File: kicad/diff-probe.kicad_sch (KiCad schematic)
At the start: 31 parts, among them IC3 LMH6702, IC4 LMH6702, IC5 LMH6702, J1 Molex 502439-0400, J3 HEADER-1X2CARD-EDGE, J4 Molex 502494-0470, X2 SMA--BU-SMA-H

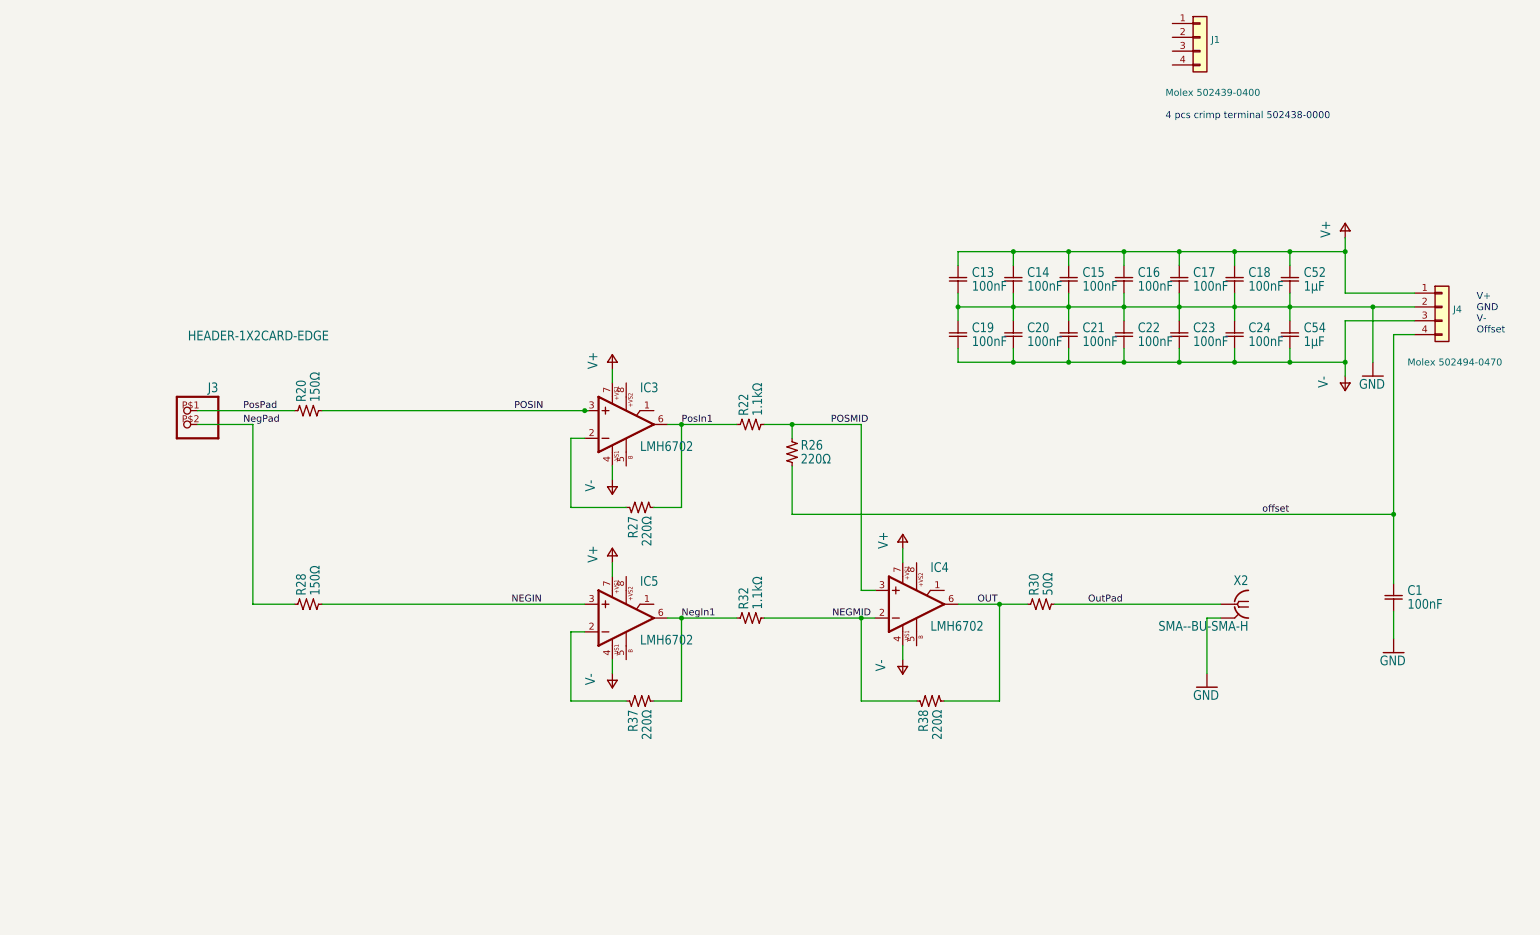
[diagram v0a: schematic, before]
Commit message: Change name for the old project to the kicad_old, remove old stored files. Create new design use new faster op-amp, and two op-amp differential input, create simulation for it. Update PCB design. Still need to design the PCB file, and check the simulation result - need some optimization.
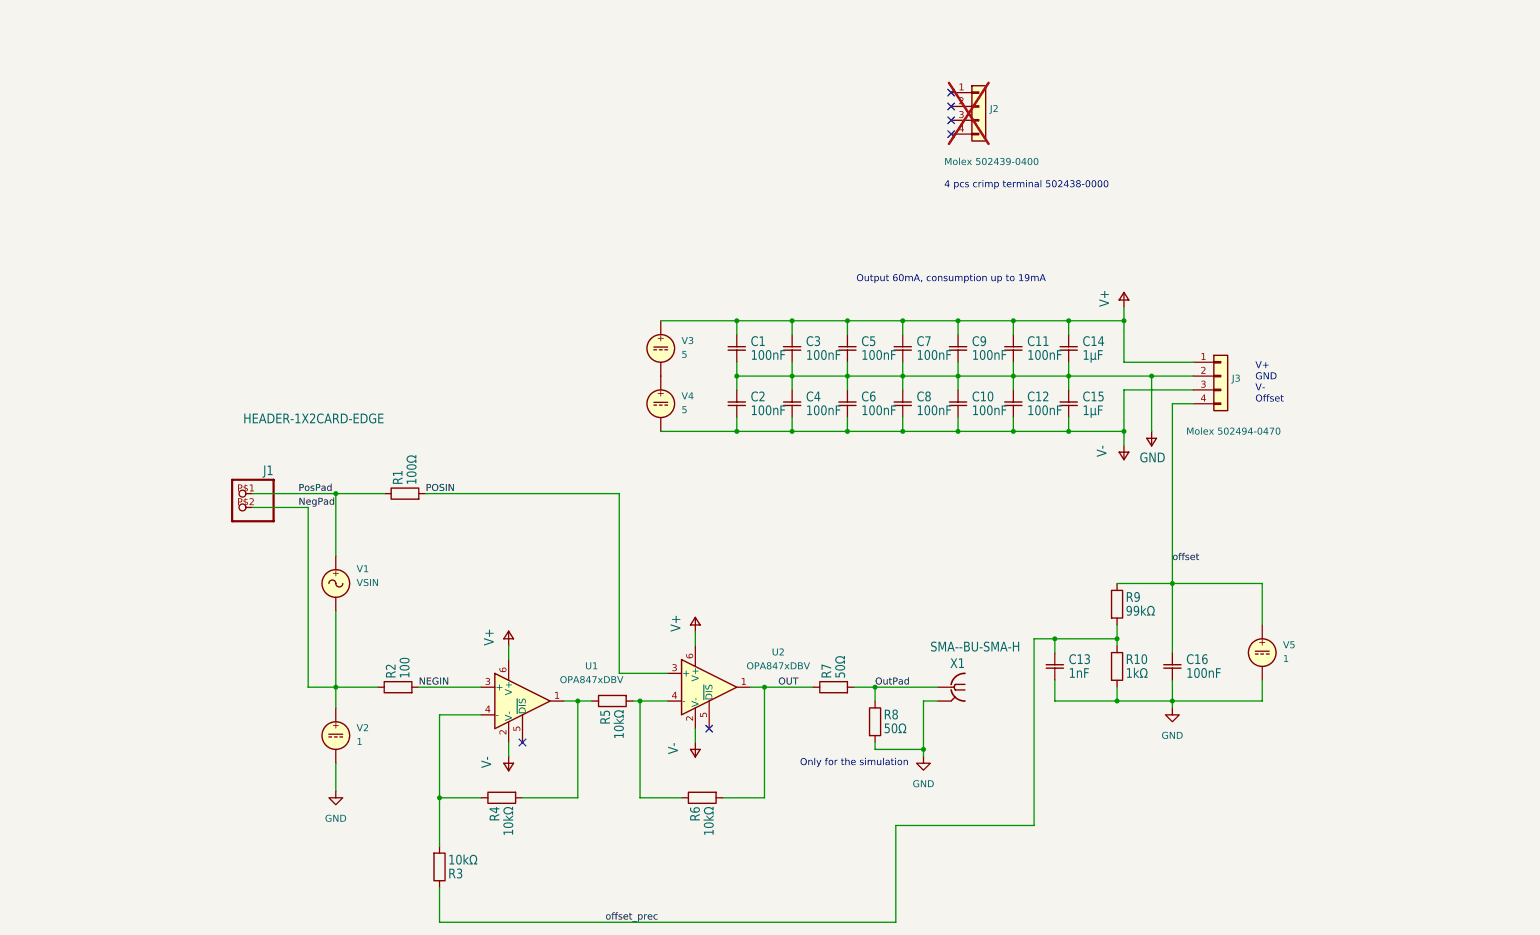
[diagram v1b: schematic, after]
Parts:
- removed IC3, IC4, IC5: LMH6702, SO08, symbol diff-probe-eagle-import:OP-AMP-8-TI
- removed R22, R32: 1.1kΩ, 0402-SQUARE, symbol diff-probe-eagle-import:R-US-0402-SQUARE
- removed R26, R27, R37: 220Ω, 0402-SQUARE, symbol diff-probe-eagle-import:R-US-0402-SQUARE
- added C13: 1nF, Capacitor_SMD:C_0402_1005Metric, symbol diff-probe-eagle-import:C-EU-0402-SQUARE
- added R10: 1kΩ, Resistor_SMD:R_0402_1005Metric, symbol Device:R
- added R3, R4, R6: 10kΩ, Resistor_SMD:R_0402_1005Metric, symbol Device:R
- added R8: 50Ω, Resistor_SMD:R_0402_1005Metric, symbol Device:R
- added R9: 99kΩ, Resistor_SMD:R_0402_1005Metric, symbol Device:R
- added U1, U2: OPA847xDBV, Package_TO_SOT_SMD:SOT-23-6, symbol Amplifier_Operational:OPA847xDBV
- added V1: VSIN, symbol Simulation_SPICE:VSIN
- added V2, V5: 1, symbol Simulation_SPICE:VDC
- added V3, V4: 5, symbol Simulation_SPICE:VDC
- C1: renamed from C13; footprint 0402-SQUARE -> Capacitor_SMD:C_0402_1005Metric
- C10: renamed from C23; footprint 0402-SQUARE -> Capacitor_SMD:C_0402_1005Metric
- C11: renamed from C18; footprint 0402-SQUARE -> Capacitor_SMD:C_0402_1005Metric
- C12: renamed from C24; footprint 0402-SQUARE -> Capacitor_SMD:C_0402_1005Metric
- C14: renamed from C52; footprint 0603 -> Capacitor_SMD:C_0402_1005Metric
- C15: renamed from C54; footprint 0603 -> Capacitor_SMD:C_0402_1005Metric
- C16: renamed from C1; footprint 0402-SQUARE -> Capacitor_SMD:C_0402_1005Metric
- C2: renamed from C19; footprint 0402-SQUARE -> Capacitor_SMD:C_0402_1005Metric
- C3: renamed from C14; footprint 0402-SQUARE -> Capacitor_SMD:C_0402_1005Metric
- C4: renamed from C20; footprint 0402-SQUARE -> Capacitor_SMD:C_0402_1005Metric
- C5: renamed from C15; footprint 0402-SQUARE -> Capacitor_SMD:C_0402_1005Metric
- C6: renamed from C21; footprint 0402-SQUARE -> Capacitor_SMD:C_0402_1005Metric
- C7: renamed from C16; footprint 0402-SQUARE -> Capacitor_SMD:C_0402_1005Metric
- C8: renamed from C22; footprint 0402-SQUARE -> Capacitor_SMD:C_0402_1005Metric
- C9: renamed from C17; footprint 0402-SQUARE -> Capacitor_SMD:C_0402_1005Metric
- J1: renamed from J3; footprint CARD_EDGE_PADS-1X2 -> Library:CARD_EDGE_PADS-1X2
- J2: renamed from J1; now not fitted; now left out of the parts list
- R1: renamed from R20; value 150Ω -> 100Ω; footprint 0402-SQUARE -> Resistor_SMD:R_0402_1005Metric; symbol diff-probe-eagle-import:R-US-0402-SQUARE -> Device:R
- R2: renamed from R28; value 150Ω -> 100; footprint 0402-SQUARE -> Resistor_SMD:R_0402_1005Metric; symbol diff-probe-eagle-import:R-US-0402-SQUARE -> Device:R
- R5: renamed from R38; value 220Ω -> 10kΩ; footprint 0402-SQUARE -> Resistor_SMD:R_0402_1005Metric; symbol diff-probe-eagle-import:R-US-0402-SQUARE -> Device:R
- R7: renamed from R30; footprint 0402-SQUARE -> Resistor_SMD:R_0402_1005Metric; symbol diff-probe-eagle-import:R-US-0402-SQUARE -> Device:R
- renumbered J4 to J3, X2 to X1
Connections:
- net GND: now also C13.P$2 (2), R10.2, R8.2, V2.2, V5.2; no longer C1.P$2 (2), C10.P$1 (1), C11.P$2 (2), C12.P$1 (1), C14.2, C15.1, C2.P$1 (1), C3.P$2 (2), C4.P$1 (1), C5.P$2 (2), C6.P$1 (1), C7.P$2 (2), C8.P$1 (1), C9.P$2 (2), J3.2 (Pin_2)
- net NEGIN: now also R2.2, U1.3 (+); no longer R2.P$2 (2)
- net NegPad: now also R2.1, V1.2, V2.1; no longer R2.P$1 (1)
- net OUT: now also R7.1, R6.2, U2.1; no longer R5.P$2 (2), R7.P$1 (1)
- net OutPad: now also R7.2, R8.1; no longer R7.P$2 (2)
- net POSIN: now also R1.2, U2.3 (+); no longer R1.P$2 (2)
- net PosPad: now also R1.1, V1.1; no longer R1.P$1 (1)
- net offset: now also R9.1, V5.1
- removed net NEGMID: R5.P$1 (1)
- net V+: no longer names the net of C1.P$1 (1), C11.P$1 (1), C14.1, C3.P$1 (1), C5.P$1 (1), C7.P$1 (1), C9.P$1 (1), J3.1 (Pin_1)
- net V+: now also V3.1
- net V-: no longer names the net of C10.P$2 (2), C12.P$2 (2), C15.2, C2.P$2 (2), C4.P$2 (2), C6.P$2 (2), C8.P$2 (2), J3.3 (Pin_3)
- net V-: now also V4.2
- new net: C1.P$2 (2), C10.P$1 (1), C11.P$2 (2), C12.P$1 (1), C14.2, C15.1, C2.P$1 (1), C3.P$2 (2), C4.P$1 (1), C5.P$2 (2), C6.P$1 (1), C7.P$2 (2), C8.P$1 (1), C9.P$2 (2), J3.2 (Pin_2)
- new net: R5.2, R6.1, U2.4 (-)
- new net: R3.2, R4.1, U1.4 (-)
- new net: R4.2, R5.1, U1.1
- new net: V3.2, V4.1
- new net offset_prec: C13.P$1 (1), R10.1, R3.1, R9.2
- no-connect marks 0 -> 6
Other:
- note added: "Only for the simulation"
- note added: "Output 60mA, consumption up to 19mA"
- title: (none) -> High speed differential probe up to 1.5GHz
- moved on the sheet: C1, C10, C11, C12, C14, C15, C16, C2, C3, C4, C5, C6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

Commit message: Update schematic using the new version of Op-amp, with high bandwidth, new topology, new DC/DC converter to create 5V power supply from 15V, and negative -5V from it.
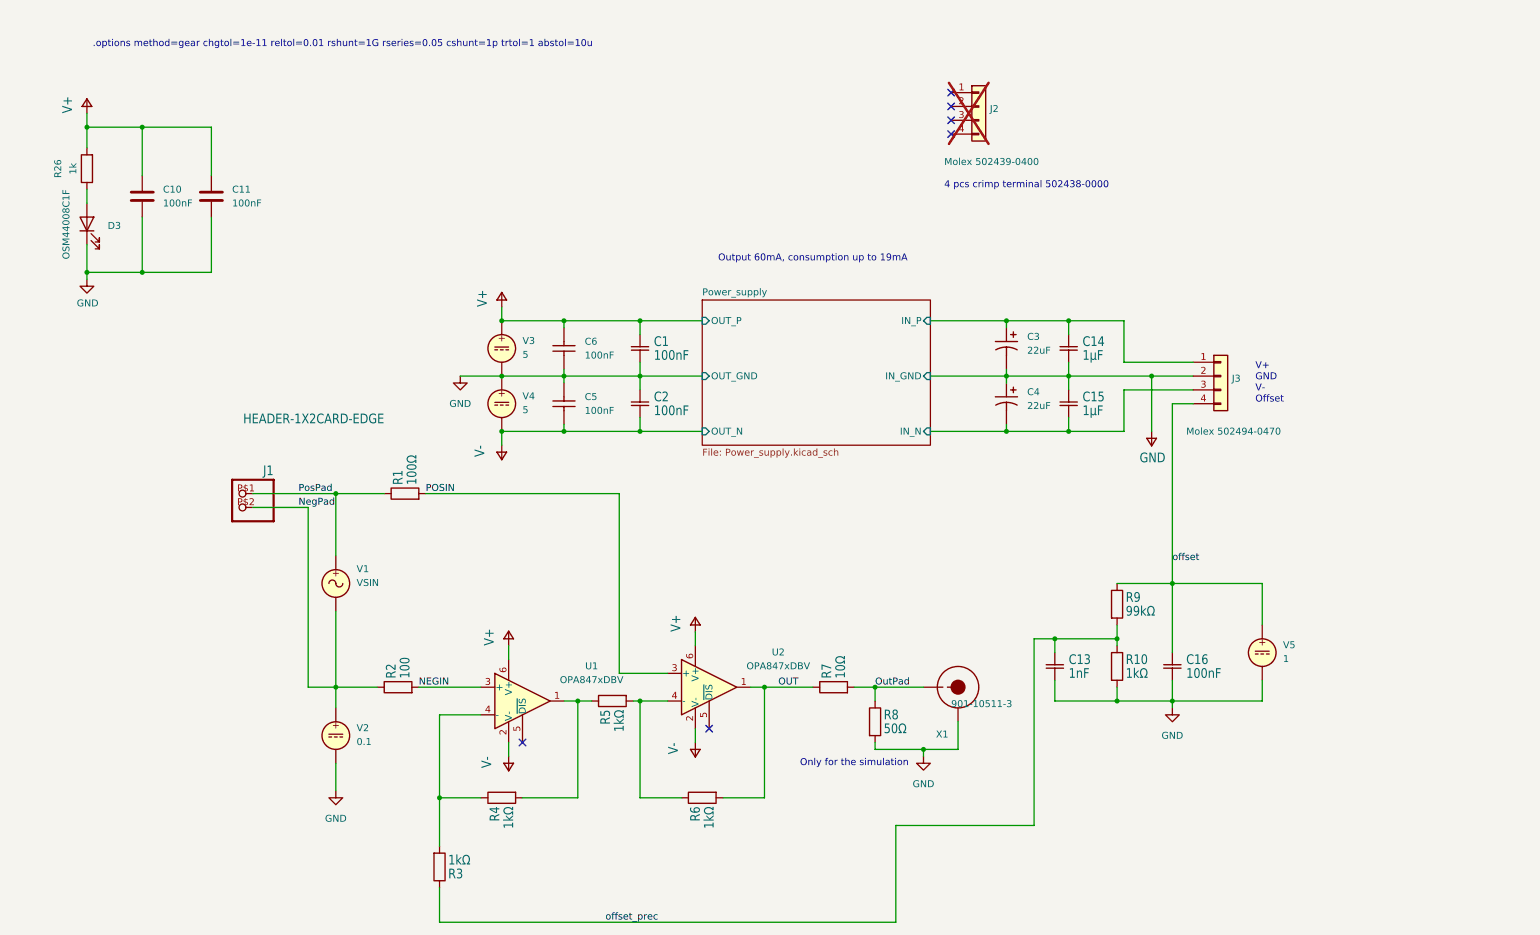
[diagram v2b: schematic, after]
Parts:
- removed C10, C11, C12, C3, C4, C5, C6, C7, C8, C9: 100nF, Capacitor_SMD:C_0402_1005Metric, symbol diff-probe-eagle-import:C-EU-0402-SQUARE
- removed X1: SMA--BU-SMA-H, Connector_Coaxial:SMA_Molex_73251-1153_EdgeMount_Horizontal, symbol diff-probe-eagle-import:SMA--BU-SMA-H
- added C10, C11: 100nF, Capacitor_SMD:C_0402_1005Metric, symbol Device:C
- added C3, C4: 22uF, Capacitor_Tantalum_SMD:CP_EIA-3528-21_Kemet-B, symbol active_probe-altium-import:root_3_T491B226K016AT
- added C5, C6: 100nF, Capacitor_SMD:C_0306_0816Metric, symbol active_probe-altium-import:root_3_TWK107B7104MVHT
- added D3: OSM44008C1F, LED_SMD:LED_OptoSupply_OSXX4008C1F_4x1.4mm_Horizontal, symbol Device:LED
- added R26: 1k, Resistor_SMD:R_0402_1005Metric, symbol Device:R
- added X1: 901-10511-3, Connector_Coaxial:901-10511-3, symbol active_probe-altium-import:root_0_901-10511-3
- R3, R4, R5, R6: value 10kΩ -> 1kΩ
- R7: value 50Ω -> 10Ω
- R8: now left out of the parts list
- V2: value 1 -> 0.1
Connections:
- net GND: now also C1.P$2 (2), C2.P$1 (1), V3.2, V4.1, C10.2, C11.2, C5.1, C6.2, D3.1 (K), X1.2
- net OutPad: now also X1.1
- net Power_supply/IN_P: now reaches C14.1, J3.1 (Pin_1)
- net Power_supply/IN_P: now also C3.1; no longer C1.P$1 (1), V3.1
- net Power_supply/IN_GND: now reaches C14.2, C15.1, J3.2 (Pin_2)
- net Power_supply/IN_GND: now also C3.2, C4.1; no longer C1.P$2 (2), C2.P$1 (1)
- net Power_supply/IN_N: now reaches C15.2, J3.3 (Pin_3)
- net Power_supply/IN_N: now also C4.2; no longer C2.P$2 (2), V4.2
- new net: C10.1, C11.1, R26.2
- new net: D3.2 (A), R26.1
- new net Power_supply/OUT_N: C2.P$2 (2), C5.2, V4.2
- new net Power_supply/OUT_P: C1.P$1 (1), C6.1, V3.1
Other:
- added sheet Power_supply (Power_supply.kicad_sch)
- note added: ".options method=gear chgtol=1e-11 reltol=0.01 rshunt=1G rseries=0.05 cshunt=1p trtol=1 abstol=10u"
- moved on the sheet: C1, C2, V3, V4

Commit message: New version at the end of the day.
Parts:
- removed C11: 100nF, Capacitor_SMD:C_0402_1005Metric, symbol Device:C
- C1, C13, C2: symbol diff-probe-eagle-import:C-EU-0402-SQUARE -> Device:C; LCSC C15195 -> (none)
- C16: symbol diff-probe-eagle-import:C-EU-0402-SQUARE -> Device:C
- renumbered X1 to J4
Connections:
- net GND: now also C1.2, C13.2, C16.2, C2.1; no longer C1.P$2 (2), C13.P$2 (2), C16.P$2 (2), C2.P$1 (1)
- net offset: now also C16.1; no longer C16.P$1 (1)
- net offset_prec: now also C13.1; no longer C13.P$1 (1)
- net Power_supply/OUT_N renamed Power_supply/V-
- net Power_supply/V-: now also C2.2; no longer C2.P$2 (2)
- net Power_supply/OUT_P renamed Power_supply/V+
- net Power_supply/V+: now also C1.1; no longer C1.P$1 (1)
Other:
- sheet Power_supply ports: added V+, V-; removed OUT_N, OUT_P
- moved on the sheet: C10, D3, R26
